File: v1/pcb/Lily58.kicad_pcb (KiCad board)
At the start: 2 copper layers, 142.5 x 106.3 mm, 261 parts, among them P4 OLED, SW1 SW_PUSH, SW10 SW_PUSH, SW11 SW_PUSH, SW12 SW_PUSH, SW13 SW_PUSH, SW14 SW_PUSH, SW15 SW_PUSH, SW16 SW_PUSH, SW17 SW_PUSH, SW18 SW_PUSH, SW19 SW_PUSH, SW2 SW_PUSH, SW20 SW_PUSH, SW21 SW_PUSH, SW22 SW_PUSH, SW23 SW_PUSH, SW24 SW_PUSH, SW25 Rotary_Encoder_Switch, SW26 SW_PUSH, SW27 SW_PUSH, SW28 SW_PUSH, SW29 SW_PUSH, SW3 SW_PUSH, SW4 SW_PUSH, SW5 SW_PUSH, SW6 SW_PUSH, SW7 SW_PUSH, SW8 SW_PUSH, SW9 SW_PUSH, U1 NiceNano

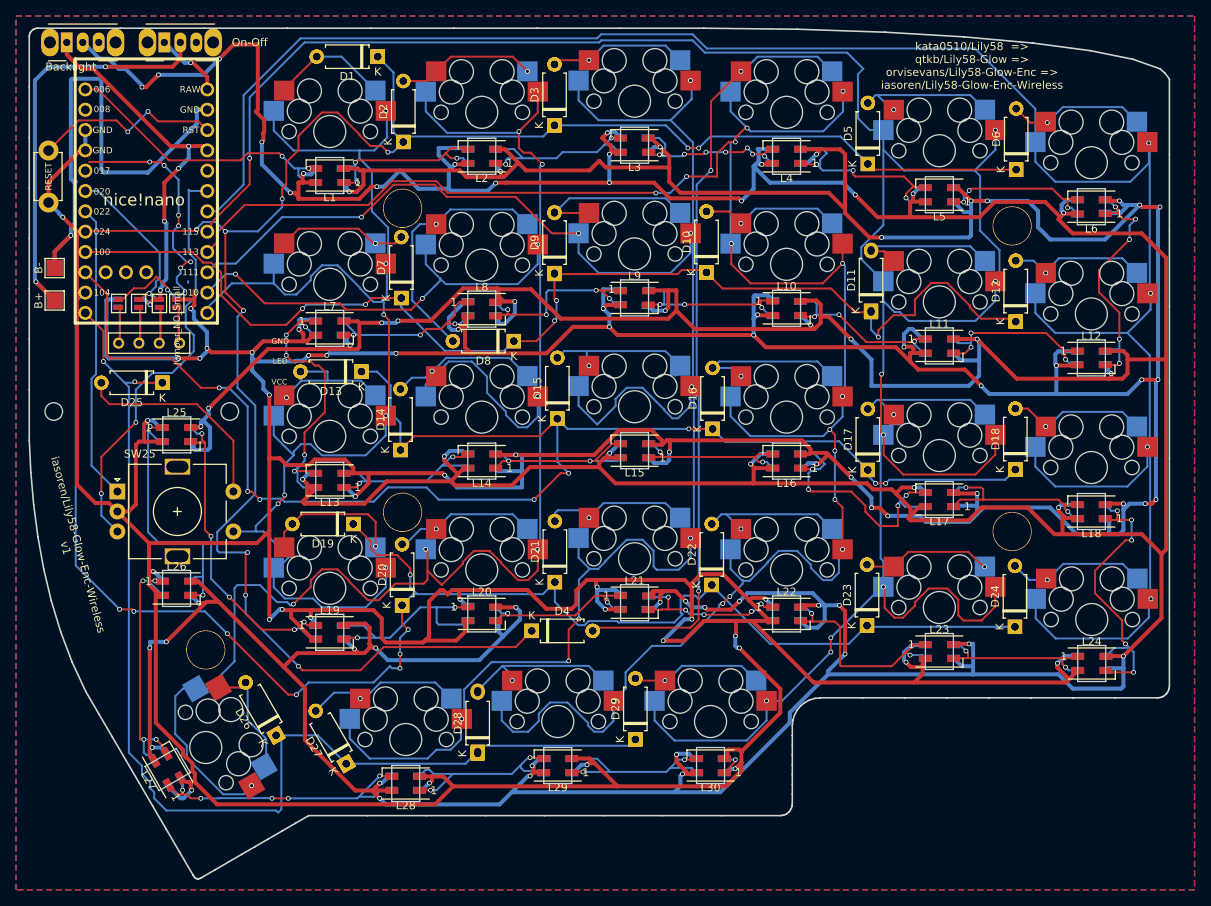
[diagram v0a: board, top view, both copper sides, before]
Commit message: Fixes to V1
Fixing V1 errors, v2 is working
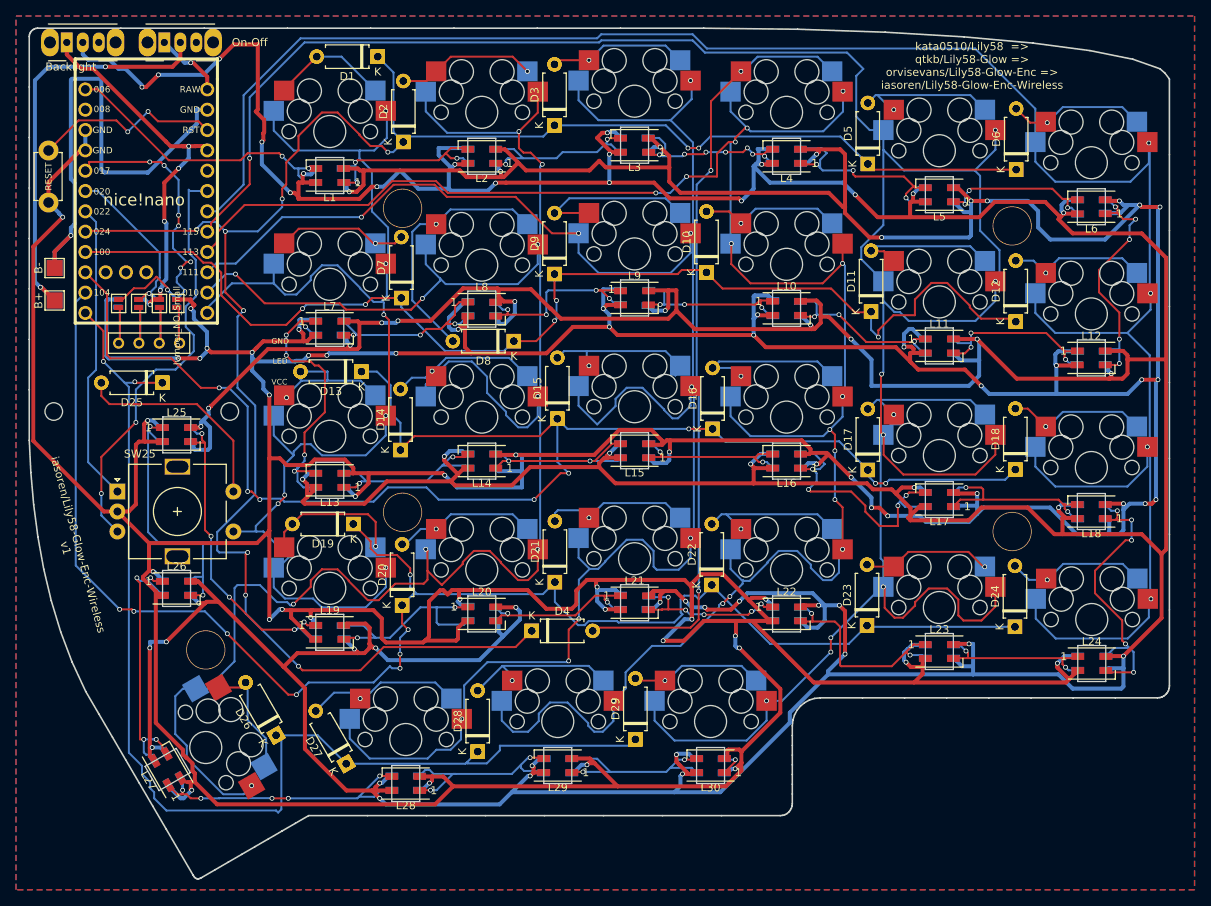
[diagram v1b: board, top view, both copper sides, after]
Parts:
- moved D28 0.25 mm to (139.0, 127.5)
- moved D11 0.13 mm to (188.2, 72.5)
- moved D9 0.13 mm to (148.6, 67.8)
- moved D11 0.08 mm to (188.2, 72.5)
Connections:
- ? pad 3: LEDunder -> Net-(L1-Pad4)
- D13 pad 1: (no net) -> row2
- D13 pad 2: (no net) -> Net-(D13-Pad2)
- D14 pad 1: (no net) -> row2
- D14 pad 2: (no net) -> Net-(D14-Pad2)
- D16 pad 1: (no net) -> row2
- D16 pad 2: (no net) -> Net-(D16-Pad2)
- D2 pad 1: (no net) -> row0
- D2 pad 2: (no net) -> Net-(D2-Pad2)
- D22 pad 2: (no net) -> Net-(D22-Pad2)
- D23 pad 1: (no net) -> row3
- D23 pad 2: (no net) -> Net-(D23-Pad2)
- D25 pad 1: (no net) -> row4
- D25 pad 2: (no net) -> Net-(D25-Pad2)
- D26 pad 1: (no net) -> row4
- D27 pad 1: (no net) -> row4
- D28 pad 1: (no net) -> row4
- D28 pad 2: (no net) -> Net-(D28-Pad2)
- D29 pad 1: (no net) -> row4
- D29 pad 2: (no net) -> Net-(D29-Pad2)
- D3 pad 1: (no net) -> row0
- D3 pad 2: (no net) -> Net-(D3-Pad2)
- D4 pad 1: (no net) -> row0
- D4 pad 2: (no net) -> Net-(D4-Pad2)
- D5 pad 1: (no net) -> row0
- D5 pad 2: (no net) -> Net-(D5-Pad2)
- D6 pad 1: (no net) -> row0
- D6 pad 2: (no net) -> Net-(D6-Pad2)
- D9 pad 1: (no net) -> row1
- D9 pad 2: (no net) -> Net-(D9-Pad2)
- L1 pad 3: LEDunder -> Net-(L1-Pad4)
- U1 pad 1: LEDunder -> Net-(L1-Pad4)
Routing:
- net Net-(L1-Pad4): track 926.8 -> 965.9 mm, vias 56 -> 58
- net LEDunder: track 36.7 -> 0.00 mm, vias 2 -> 0
- net row4: track 142.0 -> 145.4 mm
- net GND: track 1065.3 -> 1068.0 mm
- net Net-(L26-Pad1): track 31.1 -> 32.7 mm
- net SDA: track 42.0 -> 43.1 mm
- net Net-(J+1-Pad1): track 53.2 -> 52.4 mm

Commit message: Hopefully Fixed PCB
Added in the option to replace the right hand encoder with a switch, must be soldered though. Hopefully this PCB will work this time around!
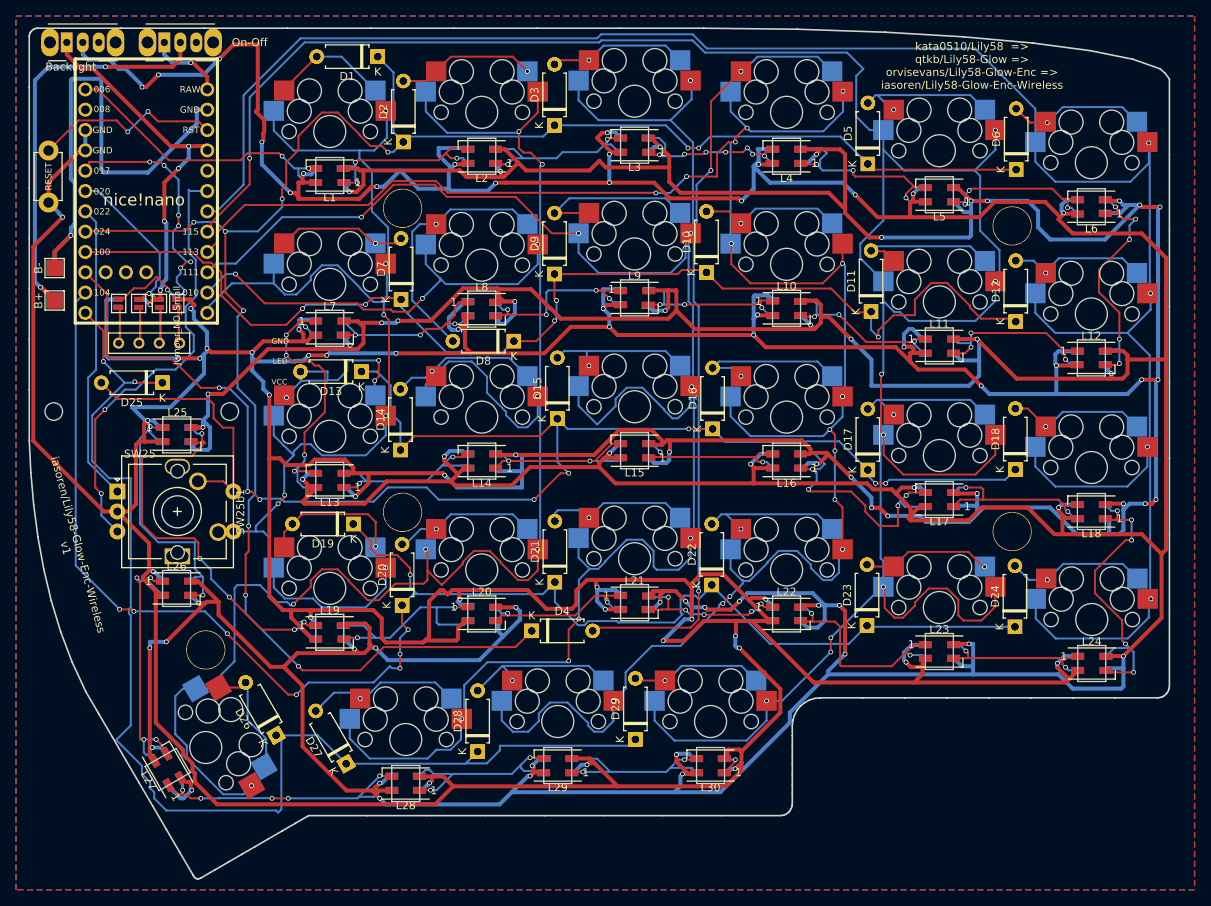
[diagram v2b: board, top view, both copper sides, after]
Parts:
- added SW25b1: SW_Cherry_MX_1.00u_PCB, Button_Switch_Keyboard:SW_Cherry_MX_1.00u_PCB, F.Cu at (106.6, 100.1)
- moved D7 0.18 mm to (129.4, 71.0) (x2)
- moved L25 0.10 mm to (101.4, 87.9)
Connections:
- D1 pad 1: (no net) -> row0
- D1 pad 2: (no net) -> Net-(D1-Pad2)
- D10 pad 1: (no net) -> row1
- D10 pad 2: (no net) -> Net-(D10-Pad2)
- D11 pad 1: (no net) -> row1
- D11 pad 2: (no net) -> Net-(D11-Pad2)
- D12 pad 1: (no net) -> row1
- D12 pad 2: (no net) -> Net-(D12-Pad2)
- D15 pad 1: (no net) -> row2
- D15 pad 2: (no net) -> Net-(D15-Pad2)
- D17 pad 1: (no net) -> row2
- D17 pad 2: (no net) -> Net-(D17-Pad2)
- D18 pad 1: (no net) -> row2
- D18 pad 2: (no net) -> Net-(D18-Pad2)
- D19 pad 1: (no net) -> row3
- D19 pad 2: (no net) -> Net-(D19-Pad2)
- D20 pad 1: (no net) -> row3
- D20 pad 2: (no net) -> Net-(D20-Pad2)
- D21 pad 1: (no net) -> row3
- D21 pad 2: (no net) -> Net-(D21-Pad2)
- D22 pad 1: (no net) -> row3
- D24 pad 1: (no net) -> row3
- D24 pad 2: (no net) -> Net-(D24-Pad2)
- D26 pad 2: (no net) -> Net-(D26-Pad2)
- D27 pad 2: (no net) -> Net-(D27-Pad2)
- D7 pad 1: (no net) -> row1
- D7 pad 2: (no net) -> Net-(D7-Pad2)
- D8 pad 1: (no net) -> row1
- D8 pad 2: (no net) -> Net-(D8-Pad2)
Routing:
- net Net-(L19-Pad1): track 40.4 -> 53.3 mm
- net col1: track 318.8 -> 311.1 mm
- net row4: track 145.4 -> 152.0 mm
- net Net-(D25-Pad2): track 26.8 -> 32.8 mm
- net Net-(D13-Pad2): track 18.7 -> 24.7 mm, vias 1 -> 3
- net row0: track 241.0 -> 235.7 mm
- net col5: track 157.4 -> 153.4 mm
- net Net-(D15-Pad2): track 21.9 -> 18.4 mm
- net Net-(L1-Pad4): track 965.9 -> 968.6 mm
- net GND: track 1068.0 -> 1065.4 mm, vias 62 -> 60
- net enc2: track 53.5 -> 54.9 mm
- net Batt+: track 8.72 -> 9.61 mm

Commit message: Keymap updates
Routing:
- net Batt-: track 62.6 -> 52.2 mm
- net Net-(L1-Pad4): track 968.6 -> 958.8 mm, vias 58 -> 56
- net SDA: track 43.1 -> 41.4 mm, vias 7 -> 2
